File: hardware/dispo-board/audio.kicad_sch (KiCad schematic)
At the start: 27 parts, among them U3 OPA1622, U4 CS5343-CZZ, U5 CS4344-CZZR

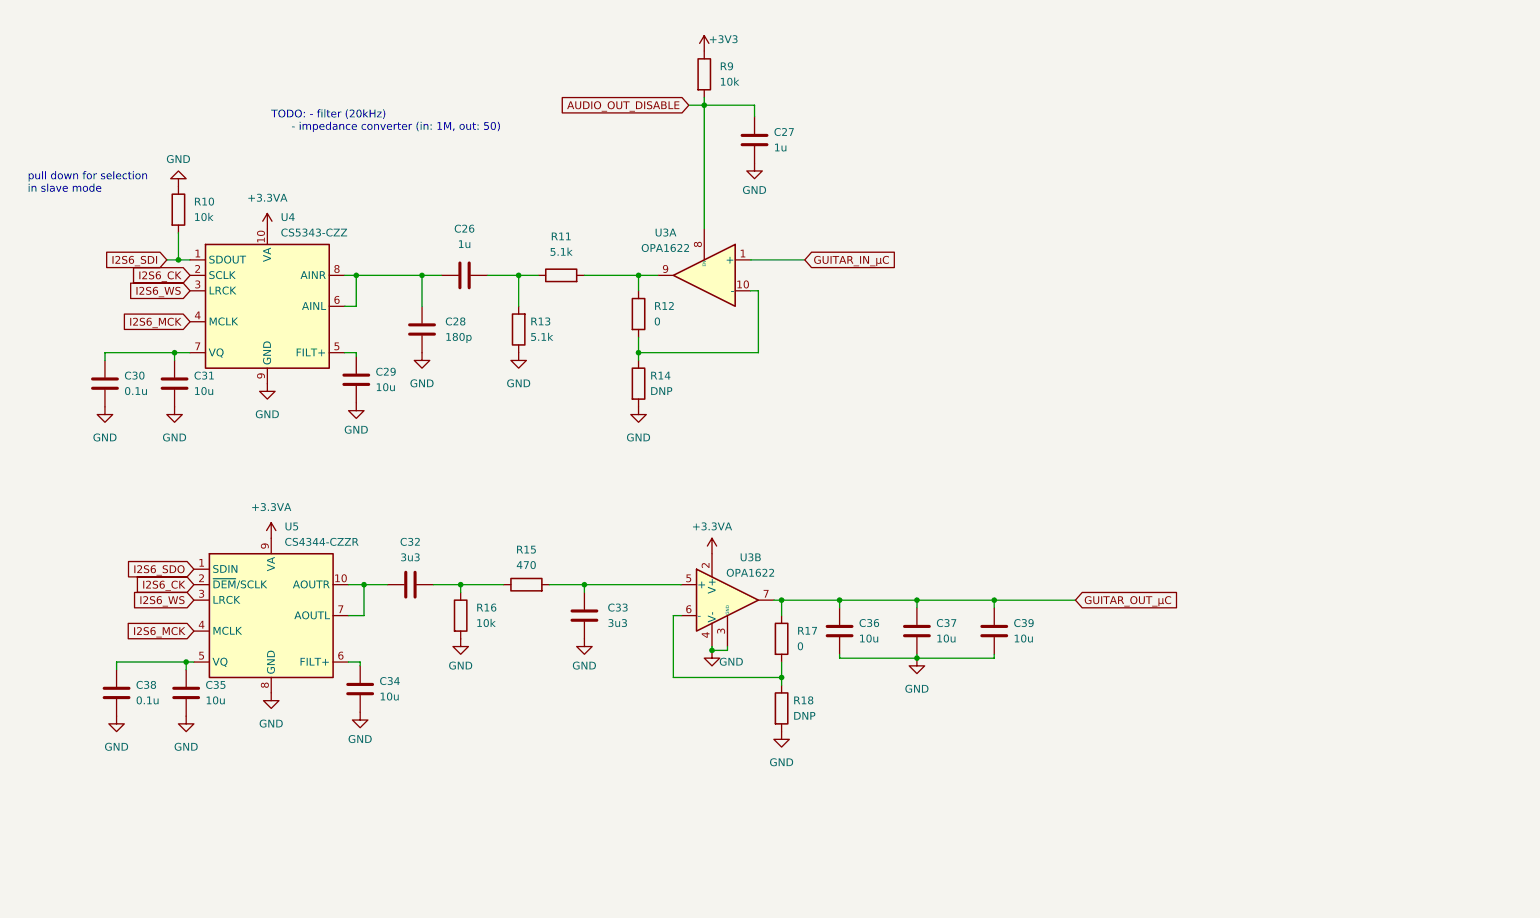
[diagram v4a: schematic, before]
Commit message: few changes supply op amp, anaolg input and output, updated footprints and mouser nrs
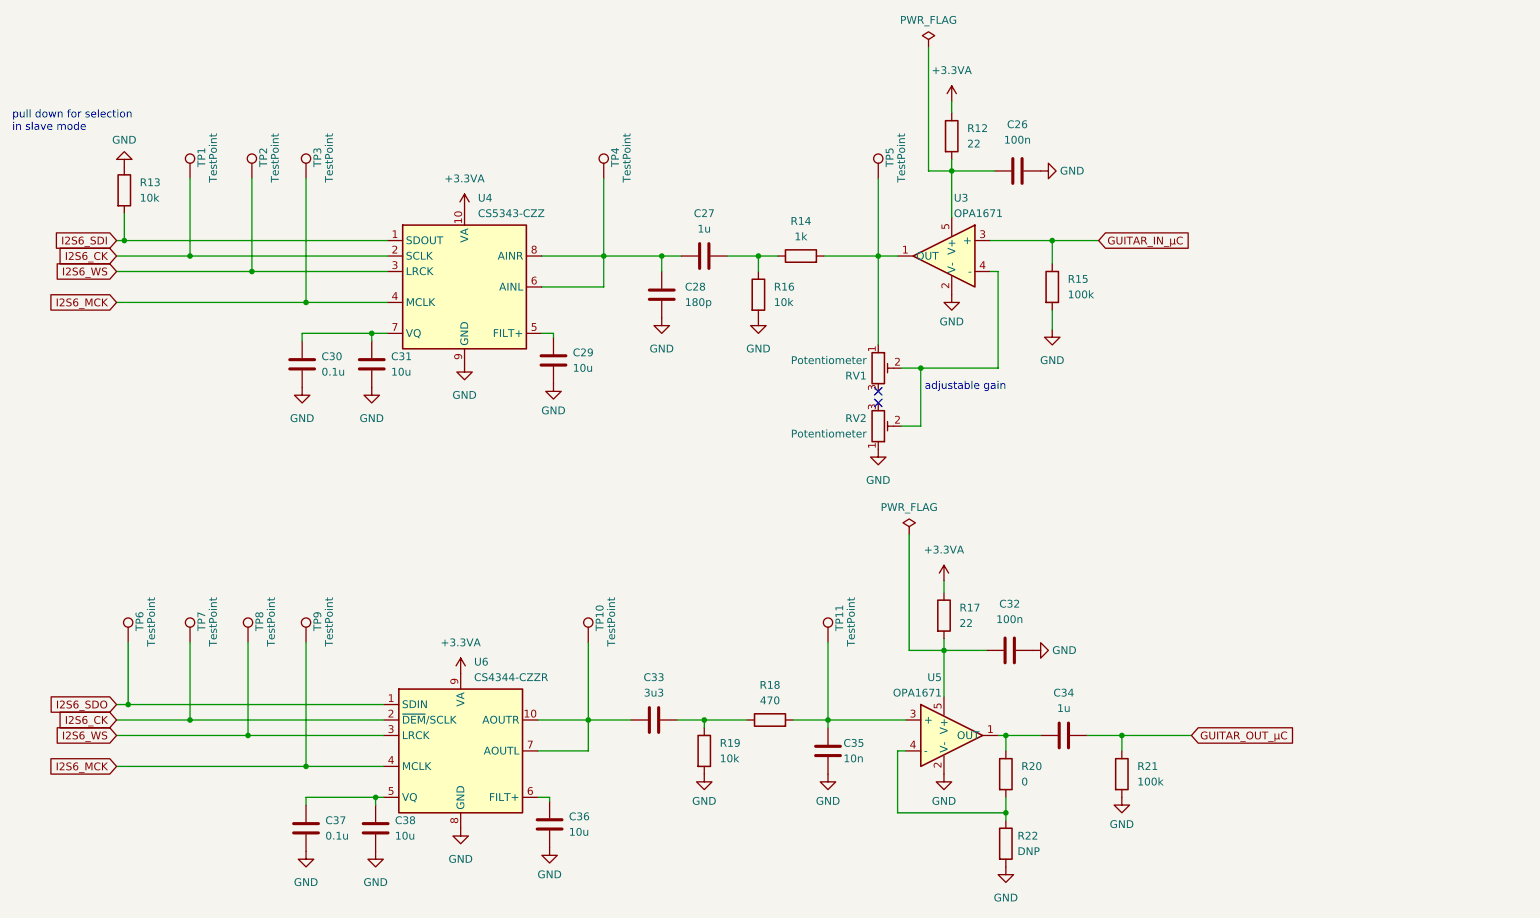
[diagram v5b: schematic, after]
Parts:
- removed C33: 3u3, Capacitor_SMD:C_0603_1608Metric, symbol Device:C
- removed C36, C37, C39: 10u, Capacitor_SMD:C_0603_1608Metric, symbol Device:C
- removed R13: 5.1k, Resistor_SMD:R_0402_1005Metric, symbol Device:R
- removed R14: DNP, Resistor_SMD:R_0402_1005Metric, symbol Device:R
- removed R9: 10k, Resistor_SMD:R_0402_1005Metric, symbol Device:R
- removed U3: OPA1622, Package_SON:Texas_S-PVSON-N10, symbol Amplifier_Audio:OPA1622
- added C32: 100n, Capacitor_SMD:C_0402_1005Metric, symbol Device:C
- added C34: 1u, Capacitor_SMD:C_1206_3216Metric, symbol Device:C
- added C35: 10n, Capacitor_SMD:C_0402_1005Metric, symbol Device:C
- added R15, R21: 100k, Resistor_SMD:R_0603_1608Metric, symbol Device:R
- added R16: 10k, Resistor_SMD:R_0402_1005Metric, symbol Device:R
- added R17: 22, Resistor_SMD:R_0603_1608Metric, symbol Device:R
- added RV1, RV2: Potentiometer, Potentiometer_SMD:Potentiometer_Bourns_3224W_Vertical, symbol Device:R_Potentiometer_Trim
- added TP1, TP10, TP11, TP2, TP3, TP4, TP5, TP6, TP7, TP8, TP9: TestPoint, TestPoint:TestPoint_Pad_D1.5mm, symbol Connector:TestPoint
- added U3, U5: OPA1671, Package_TO_SOT_SMD:SOT-23-5, symbol MySymbols:OPAmp
- C26: value 1u -> 100n; footprint Capacitor_SMD:C_0603_1608Metric -> Capacitor_SMD:C_0402_1005Metric; MOUSER_NR 81-GRM185R61C105KE4J -> 81-GRM15R61A104KA01J
- C27: footprint Capacitor_SMD:C_0603_1608Metric -> Capacitor_SMD:C_1206_3216Metric; MOUSER_NR 81-GRM185R61C105KE4J -> 598-FCA1206A105M-H3
- C33: renamed from C32; MOUSER_NR 81-GCJ188L8EC335KE8D -> 232-16MU335MB33225
- R12: value 0 -> 22; footprint Resistor_SMD:R_0402_1005Metric -> Resistor_SMD:R_0603_1608Metric; MOUSER_NR 710-560112110001 -> 652-CHP0603QJW-220E
- R14: renamed from R11; value 5.1k -> 1k; MOUSER_NR 71-TNPW04025K10BYEP -> (none)
- renumbered C34 to C36, C38 to C37, C35 to C38, R10 to R13, R15 to R18, R16 to R19, R17 to R20, R18 to R22, U5 to U6
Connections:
- net AUDIO_OUT_DISABLE is gone; now on an unnamed net: C27.2
- net +3.3VA: now also R12.1, R17.1
- net GND: now also C26.2, C32.2, C35.2, R15.2, R16.2, R21.2, RV2.1, U3.2 (V-), U5.2 (V-); no longer C27.1
- net GUITAR_IN_µC: now also R15.1, U3.3 (+)
- net GUITAR_OUT_µC: now also C34.2, R21.1; no longer R20.1
- net I2S6_CK: now also TP1.1, TP7.1
- net I2S6_MCK: now also TP3.1, TP9.1
- net I2S6_SDO: now also TP6.1
- net I2S6_WS: now also TP2.1, TP8.1
- net at R14.2: now also RV1.1, TP5.1, U3.1 (OUT); no longer R12.1
- net at R12.2: now also C26.1, U3.5 (V+)
- net at C33.1, U6.10 (AOUTR), U6.7 (AOUTL): now also TP10.1
- net at C28.1, U4.6 (AINL), U4.8 (AINR): now also C27.1, TP4.1; no longer C26.1
- net at R14.1: now also R16.1; no longer C26.2
- net at R18.2: now also C35.1, TP11.1, U5.3 (+)
- net at R20.2, R22.1: now also U5.4 (-)
- new net: RV1.2, RV2.2, U3.4 (-)
- new net: C32.1, R17.2, U5.5 (V+)
- new net: C34.1, R20.1, U5.1 (OUT)
- no-connect marks 0 -> 2
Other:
- note added: "adjustable gain"
- note removed: "TODO: - filter (20kHz) - impedance converter (in: 1M, out: 50)"
- moved on the sheet: C28, C29, C30, C31, C33, C36, C37, C38, R13, R14, R18, R19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

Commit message: updated footprints, pcb
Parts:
- renumbered C26 to C24, C27 to C25, C28 to C26, C29 to C27, C30 to C28, C31 to C29, C32 to C30, C33 to C31, C34 to C32, C35 to C33, C36 to C34, C37 to C35, C38 to C36

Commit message: pcb and parts ordered like this
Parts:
- C28, C35: value 0.1u -> 100n
- R14: MOUSER_NR (none) -> 71-CRCW0402-1.0K-E3
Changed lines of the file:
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@@
       (effects (font (size 1.27 1.27)) (justify left))
     )
-    (property "Value" "0.1u" (at 72.39 148.59 0)
+    (property "Value" "100n" (at 72.39 148.59 0)
       (effects (font (size 1.27 1.27)) (justify left))
     )
@@
       (effects (font (size 1.27 1.27)) (justify left))
     )
-    (property "Value" "0.1u" (at 71.755 72.39 0)
+    (property "Value" "100n" (at 71.755 72.39 0)
       (effects (font (size 1.27 1.27)) (justify left))
     )
@@
       (effects (font (size 1.27 1.27)) hide)
     )
-    (property "MOUSER_NR" "" (at 150.495 53.34 90)
-      (effects (font (size 1.27 1.27)) hide)
-    )
+    (property "MOUSER_NR" " 71-CRCW0402-1.0K-E3 " (at 150.495 53.34 90)
+      (effects (font (size 1.27 1.27)) hide)
+    )
